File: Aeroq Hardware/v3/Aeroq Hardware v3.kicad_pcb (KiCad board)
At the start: 2 copper layers, 45 x 45 mm, 56 parts, among them Q1 Si1308EDL, U2 ESP32-C3-MINI-1-N4, U3 AMS1117-3.3, U4 SCD40-D-R1

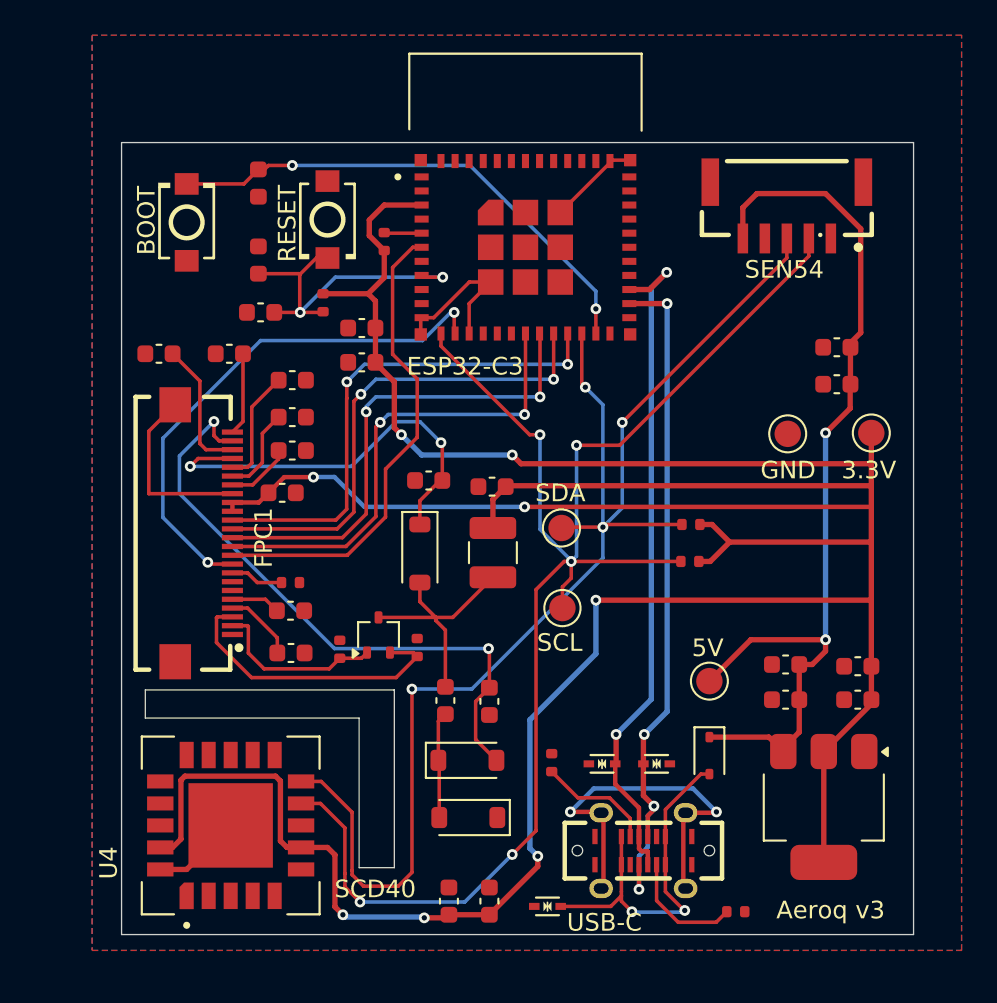
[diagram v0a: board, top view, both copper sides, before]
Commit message: KiCad schematic and PCB updates
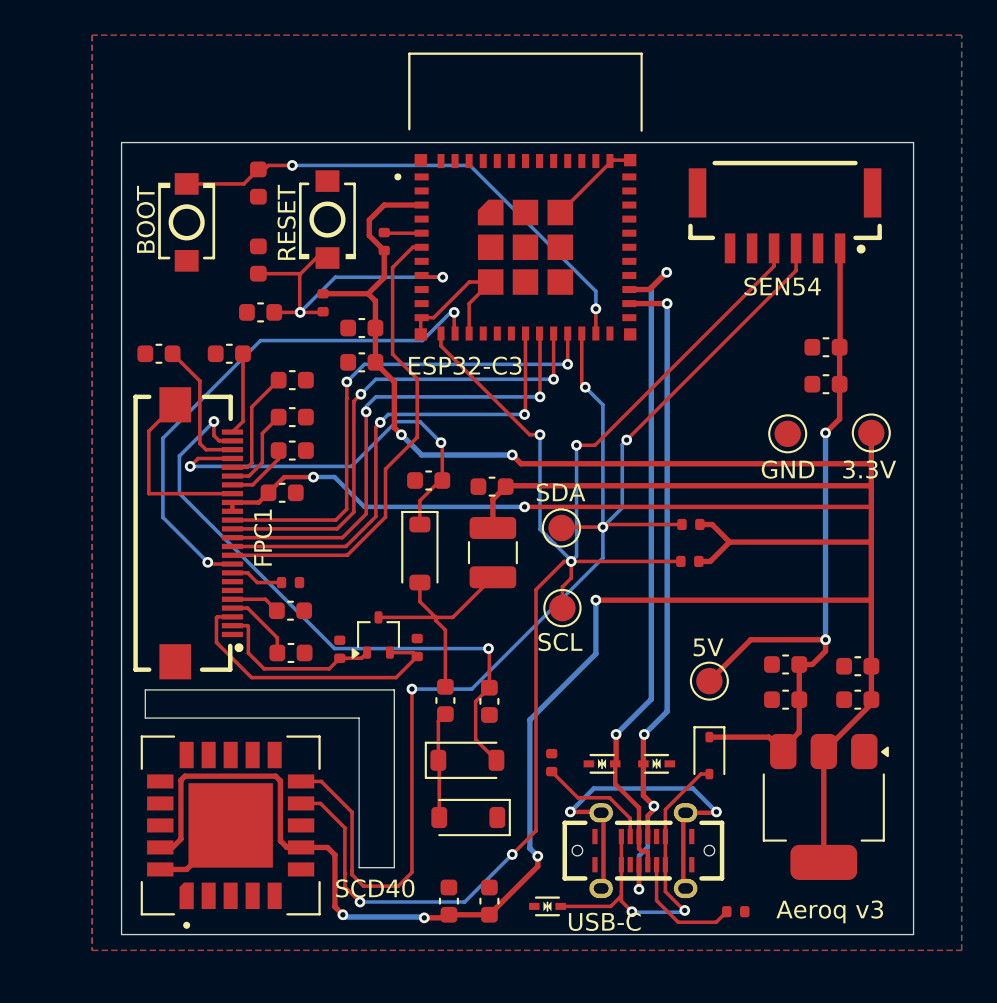
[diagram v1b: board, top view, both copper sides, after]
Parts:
- U5: footprint JST SM05B-GHS-TB(LF)(SN):CONN-SMD_5P-P1.25_SM05B-GHS-TB-LF-SN -> XUNPU WAFER-GH1.25-6PWB:CONN-SMD_6P-P1.25_XUNPU_WAFER-GH1.25-6PWB
- moved C10 0.62 mm to (127.0, 85.6)
- moved C11 0.62 mm to (127.0, 87.7)
- moved U5 0.60 mm to (124.7, 78.4)
- renumbered D6 to D5, D7 to D6, D8 to D7, R11 to R10, R6 to R5, R7 to R6, R8 to R7, R10 to R9
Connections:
- U5 pad 1: GND -> +5V
- U5 pad 2: SCL -> GND
- U5 pad 4: GND -> SCL
- U5 pad 5: +5V -> GND
- U5 pad 6: GND -> unconnected-(U5-Pad6)
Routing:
- net +5V: track 53.7 -> 42.5 mm
- net SCL: track 86.4 -> 84.2 mm

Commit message: add my customizations
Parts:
- removed FPC1: ~, Project Footprints:FPC-SMD_24P-P0.50_FPC-05FB-24PH20
- removed L1: 10uH/1A, Inductor_SMD:L_1210_3225Metric
- removed R10: 0.47, Resistor_SMD:R_0402_1005Metric
- removed SW1, SW2: ~, Project Footprints:SW-SMD_L3.9-W3.0-P4.45
- removed TP1, TP2, TP3, TP4, TP5: TestPoint, TestPoint:TestPoint_Pad_D1.5mm
- removed U4: SCD40-D-R1, Project Footprints:XDCR_SCD40-D-R1
- removed U5: ~, XUNPU WAFER-GH1.25-6PWB:CONN-SMD_6P-P1.25_XUNPU_WAFER-GH1.25-6PWB
- added C26: 4.7uF_0603_25V, Capacitor_SMD:C_0603_1608Metric, F.Cu at (127.2, 101.6)
- added D8: Green LED, LED_SMD:LED_1206_3216Metric, F.Cu at (122.7, 95.5)
- added FID1: Fiducial, Fiducial:Fiducial_0.5mm_Mask1.5mm, F.Cu at (130.2, 93.0)
- added FID2: Fiducial, Fiducial:Fiducial_0.5mm_Mask1.5mm, F.Cu at (100.8, 117.1)
- added FID3: Fiducial, Fiducial:Fiducial_0.5mm_Mask1.5mm, F.Cu at (88.3, 75.3)
- added J1: 2x4 male header 2.54 mm, Connector_PinHeader_2.54mm:PinHeader_2x04_P2.54mm_Vertical_SMD, B.Cu at (122.5, 94.1)
- added J2: USB4120-03-C, 2s_connectors:GCT_USB4120-03-C_REVA, F.Cu at (116.7, 114.1)
- added J3: SM06B-GHS-TB, Connector_JST:JST_GH_SM06B-GHS-TB_1x06-1MP_P1.25mm_Horizontal, F.Cu at (124.8, 78.0)
- added J4: FH12A-24S-0.5SH(55), 2s_connectors:Hirose_FH12-24S-0.5SH_1x24-1MP_P0.50mm_Horizontal_INVERTED, F.Cu at (91.9, 96.2)
- added L2: 10 uH, Inductor_SMD:L_Wuerth_MAPI-3020, F.Cu at (108.7, 97.3)
- added R12: 5.1k_0603, Resistor_SMD:R_0603_1608Metric, F.Cu at (111.0, 111.0)
- added R13: 5.1k_0603, Resistor_SMD:R_0603_1608Metric, F.Cu at (123.2, 117.8)
- added R8: 10k_0603, Resistor_SMD:R_0603_1608Metric, F.Cu at (97.0, 98.5)
- added S1: B3U-1000P, Button_Switch_SMD:SW_SPST_B3U-1000P, F.Cu at (90.6, 78.4)
- added S2: B3U-1000P, Button_Switch_SMD:SW_SPST_B3U-1000P, F.Cu at (96.9, 78.4)
- C1, C6, C9: value 10uf/25V -> 4.7uF_0603_25V
- C10, C12, C13, C14, C16, C17, C18, C19, C23, C24: value 4.7uf/25V -> 4.7uF_0603_25V
- C11, C15, C2, C3, C5, C7, C8: value 0.1uf/50V -> 100nF_0603_16V
- C20, C21, C22, C25: value 1uf/50V -> 1uF_0603_25V
- C4: value 1uf/50V -> 4.7uF_0603_25V
- D1: value 1N5819WS -> MBR0530; footprint Diode_SMD:D_SOD-323 -> Diode_SMD:D_SOD-123
- D2: value ~ -> SMAJ5.0CA; footprint Project Footprints:SOD-523_L1.2-W0.8-LS1.6-BI -> Diode_SMD:D_SMA
- D3, D4: value ~ -> ESD321DYAR; footprint Project Footprints:SOD-523_L1.2-W0.8-LS1.6-BI -> Package_TO_SOT_SMD:SOT-523
- R1, R2, R5, R6, R9: value 10k -> 10k_0603; footprint Resistor_SMD:R_0402_1005Metric -> Resistor_SMD:R_0603_1608Metric
- R3: value 5k -> 0.47R_0603; footprint Resistor_SMD:R_0402_1005Metric -> Resistor_SMD:R_0603_1608Metric
- R4: value 5k -> 3Ω_0603; footprint Resistor_SMD:R_0402_1005Metric -> Resistor_SMD:R_0603_1608Metric; moved to B.Cu
- R7: value 3 -> 2.2k_0603; footprint Resistor_SMD:R_0402_1005Metric -> Resistor_SMD:R_0603_1608Metric
- U1: value ~ -> TLV76133DCY; footprint Project Footprints:TYPE-C-SMD_USB4120-03-C -> Package_TO_SOT_SMD:SOT-223-3_TabPin2
- U2: footprint Project Footprints:XCVR_ESP32-C3-MINI-1-N4 -> 2s_misc:XCVR_ESP32-C3-MINI-1-N4
- U3: value AMS1117-3.3 -> SCD40-D-R2; footprint Package_TO_SOT_SMD:SOT-223-3_TabPin2 -> Sensor:Sensirion_SCD4x-1EP_10.1x10.1mm_P1.25mm_EP4.8x4.8mm
- moved C4 38.0 mm to (127.2, 103.7)
- moved U3 33.5 mm to (93.4, 112.8), turned to 90 degrees
- moved R3 28.7 mm to (97.0, 103.5), turned to 0 degrees
- moved R7 27.2 mm to (122.7, 91.2), turned to -90 degrees
- moved R5 23.8 mm to (100.4, 112.3), turned to -90 degrees
- moved R6 22.7 mm to (102.7, 111.1), turned to -90 degrees
- moved R4 18.0 mm to (97.0, 98.5), turned to 180 degrees
- moved D2 14.0 mm to (111.6, 103.5), turned to -90 degrees
- moved U1 10.8 mm to (127.1, 111.6), turned to -90 degrees
- moved C2 9.63 mm to (99.8, 76.9), turned to 90 degrees
- moved R2 9.04 mm to (93.3, 82.4), turned to 180 degrees
- moved C1 7.67 mm to (101.3, 76.9), turned to 90 degrees
- moved C9 5.80 mm to (123.5, 101.6), turned to 180 degrees
- moved D1 4.99 mm to (118.1, 104.4)
- moved C5 4.89 mm to (99.3, 82.5), turned to 180 degrees
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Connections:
- net GDR renamed /Display/GDR
- net GPIO2 renamed Net-(U2-IO2)
- net GPIO9 renamed /Microcontroller/GPIO9
- net PREVGH renamed /Display/PREVGH
- net PREVGL renamed /Display/PREVGL
- C1 pad 1: GND -> +3.3V
- C1 pad 2: +3.3V -> GND
- C4 pad 2: CHIP_PU -> +3.3V
- C5 pad 1: CHIP_PU -> /Microcontroller/CHIP_PU
- C9 pad 2: +3.3V -> +5V
- D3 pad 1: GND -> /USB-C/D-
- D3 pad 2: D- -> GND
- D4 pad 1: GND -> /USB-C/D+
- D4 pad 2: D+ -> GND
- Q1 pad 2: RESE -> /Display/RESE
- R1 pad 1: CHIP_PU -> /Microcontroller/CHIP_PU
- R3 pad 1: GND -> /Display/RESE
- R3 pad 2: Net-(U1-CC2) -> GND
- R4 pad 2: Net-(U1-CC1) -> Net-(J4-Pin_8)
- R5 pad 1: SCL -> /Microcontroller/SCL
- R6 pad 1: SDA -> /Microcontroller/SDA
- R7 pad 1: Net-(FPC1-Pad8) -> +3.3V
- R7 pad 2: GND -> Net-(D8-A)
- U2 pad 12: SCL -> /Microcontroller/SCL
- U2 pad 13: BUSY -> /Display/BUSY
- U2 pad 16: unconnected-(U2-IO10-Pad16) -> /Microcontroller/GPIO10
- U2 pad 18: DC -> /Display/D/C
- U2 pad 19: CS -> /Display/CS
- U2 pad 20: SCLK -> /Display/SCLK
- U2 pad 21: SDI -> /Display/SDI
- U2 pad 22: SDA -> /Microcontroller/SDA
- U2 pad 26: D- -> /USB-C/D-
- U2 pad 27: D+ -> /USB-C/D+
- U2 pad 30: unconnected-(U2-RXD0-Pad30) -> /Microcontroller/RXD
- U2 pad 31: unconnected-(U2-TXD0-Pad31) -> /Microcontroller/TXD
- U2 pad 6: RES -> /Display/RES
- U2 pad 8: CHIP_PU -> /Microcontroller/CHIP_PU
- U3 pad 1: GND -> (no net)
- U3 pad 2: +3.3V -> (no net)
- U3 pad 3: +5V -> (no net)
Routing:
- net +3.3V: track 212.5 -> 45.0 mm, vias 8 -> 16
- net SCL: track 84.2 -> 0.00 mm, vias 5 -> 0
- net /Microcontroller/SCL: track 0.00 -> 75.9 mm, vias 0 -> 9
- net SDA: track 75.8 -> 0.00 mm, vias 4 -> 0
- net /Microcontroller/SDA: track 0.00 -> 69.5 mm, vias 0 -> 8
- net /USB-C/D+: track 0.00 -> 40.7 mm, vias 0 -> 2
- net D-: track 39.9 -> 0.00 mm, vias 4 -> 0
- net /USB-C/D-: track 0.00 -> 39.1 mm, vias 0 -> 2
- net D+: track 38.4 -> 0.00 mm, vias 2 -> 0
- net /Display/BUSY: track 0.00 -> 32.7 mm, vias 0 -> 4
- net BUSY: track 30.3 -> 0.00 mm, vias 2 -> 0
- net /Display/SDI: track 0.00 -> 29.2 mm, vias 0 -> 2
- net SDI: track 28.7 -> 0.00 mm, vias 2 -> 0
- net /Display/SCLK: track 0.00 -> 28.5 mm, vias 0 -> 2
- net /Display/CS: track 0.00 -> 28.3 mm, vias 0 -> 2
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- added copper zone on B.Cu, net +3.3V
- removed copper zone on B.Cu, net GND
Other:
- outline, holes or cut-outs redrawn
- rule pad_to_mask_clearance: 0 -> 0.0508
- board text removed: "3.3V"
- board text removed: "5V"
- board text removed: "Aeroq v3"
- board text removed: "ESP32-C3"
- board text removed: "GND"
- board text removed: "SCD40"
- board text removed: "SCL"
- board text removed: "SDA"
- board text removed: "SEN54"
- board text removed: "USB-C"
